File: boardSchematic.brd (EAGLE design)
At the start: 100 x 80 mm, 63 parts, among them IC2 TP4056, Q1 BC817-40SMD, Q2 BC817-40SMD, Q3 BC817-40SMD

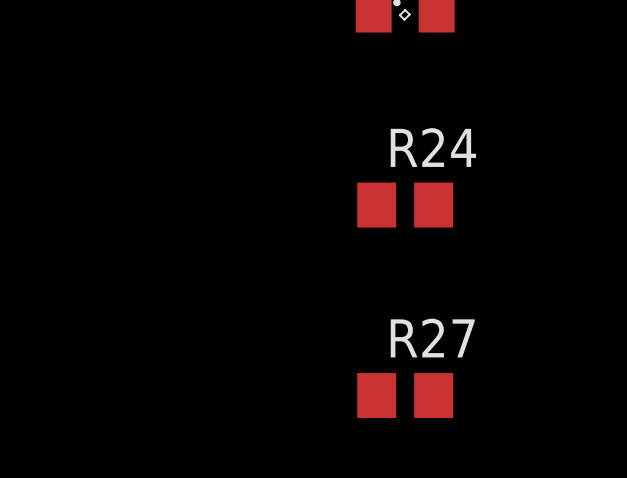
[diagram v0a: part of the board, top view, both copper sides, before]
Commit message: Added on/off switch
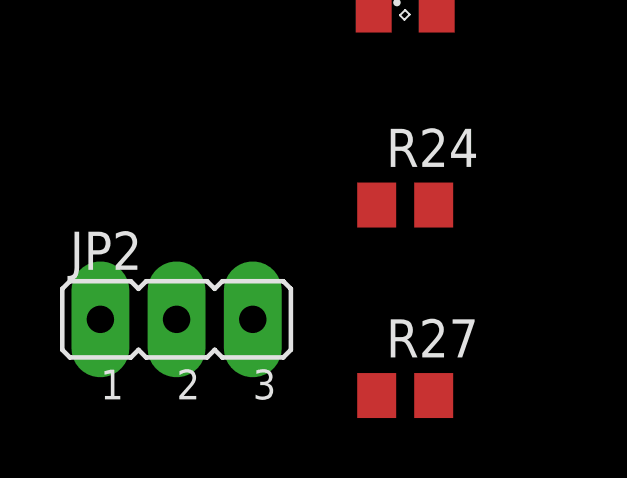
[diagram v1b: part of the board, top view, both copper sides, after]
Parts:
- added JP2: (no value), jumper:JP2
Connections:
- new net N$28: JP2.2, PAD1.1
- net VCC: now also JP2.1; no longer PAD1.1
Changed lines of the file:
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@@
 <element name="R24" library="rcl" package="R0805" value="103" x="-193.04" y="-275.59"/>
 <element name="R27" library="rcl" package="R0805" value="103" x="-193.04" y="-281.94"/>
+<element name="JP2" library="jumper" package="JP2" value="" x="-200.66" y="-279.4"/>
 </elements>
 <signals>
@@
 </signal>
 <signal name="VCC">
-<contactref element="PAD1" pad="1"/>
 <contactref element="U1" pad="3"/>
 <contactref element="C1" pad="1"/>
@@
 <contactref element="R17" pad="1"/>
 <contactref element="SG1" pad="+"/>
+<contactref element="JP2" pad="1"/>
+<wire x1="-168.91" y1="-214.63" x2="-203.2" y2="-279.4" width="0" layer="19" extent="1-1"/>
 <wire x1="-179.222" y1="-179.07" x2="-168.91" y2="-214.63" width="0" layer="19" extent="1-1"/>
 <wire x1="-179.222" y1="-173.99" x2="-179.222" y2="-179.07" width="0" layer="19" extent="1-1"/>
@@
 <wire x1="-25.08" y1="34.29" x2="-48.05" y2="-6.985" width="0" layer="19" extent="1-1"/>
 <wire x1="-14.1986" y1="32.4612" x2="-25.08" y2="34.29" width="0" layer="19" extent="1-1"/>
-<wire x1="-40.64" y1="44.45" x2="-25.08" y2="34.29" width="0" layer="19" extent="1-1"/>
 </signal>
 <signal name="+5V">
@@
 <wire x1="-186.055" y1="-235.0262" x2="-194.09" y2="-269.24" width="0" layer="19" extent="1-1"/>
 </signal>
+<signal name="N$28">
+<contactref element="JP2" pad="2"/>
+<contactref element="PAD1" pad="1"/>
+<wire x1="-40.64" y1="44.45" x2="-200.66" y2="-279.4" width="0" layer="19" extent="1-1"/>
+</signal>
 </signals>

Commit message: First guess of routing
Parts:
- removed LED1: RD, led:SML0805
- removed LED2, LED4: GR, led:SML0805
- removed R10, R9: 103, rcl:R0805
- removed R19, R20, R21, R23: 102, rcl:R0805
- moved JP2 443.0 mm to (68.6, 72.4)
- moved R24 366.0 mm to (25.6, 17.9)
- moved R27 363.6 mm to (30.6, 4.81), turned to 180 degrees
- moved Q3 361.4 mm to (19.3, 69.2)
- moved R26 356.1 mm to (35.6, 10.2)
- moved Q1 355.5 mm to (89.6, 40.0)
- moved R18 350.7 mm to (95.6, 40.6)
- moved C7 350.6 mm to (41.9, 11.4)
- moved R17 344.3 mm to (94.9, 36.2)
- moved C6 342.9 mm to (41.9, 7.62)
- moved LED8 340.5 mm to (12.2, 2.43)
- moved SG1 339.3 mm to (9.43, 71.6)
- moved U$2 332.8 mm to (34.9, 18.1)
- moved LED7 331.4 mm to (91.5, 53.1), turned to 270 degrees
- moved Q4 329.7 mm to (41.6, 1.54)
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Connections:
- removed net N$1: Q2.B, R21.2
- removed net N$10: IC2.6, LED2.C
- removed net N$2: LED1.A, R9.1
- removed net N$21: Q3.B, R23.2
- removed net N$26: LED4.A, R20.1
- removed net N$29: MEGA328.2, R20.2
- removed net N$4: Q1.B, R19.2
- removed net N$6: LED2.A, R10.1
- removed net N$8: IC2.7, LED1.C
- net BZR: now also Q3.B; no longer R23.1
- net GND: no longer LED4.C
- net GR: now also Q2.B; no longer R21.1
- net N$14: no longer R10.2, R9.2
- net RD: now also Q1.B; no longer R19.1
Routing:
- net N$1: track 0.00 -> 136.0 mm
- net N$2: track 0.00 -> 96.0 mm
- net N$4: track 0.00 -> 84.0 mm
- net +3V3: track 0.00 -> 16.4 mm
- net GND: track 0.00 -> 13.2 mm

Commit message: Test 2
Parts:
- moved C4 23.4 mm to (72.5, 75.4), turned to 90 degrees
- moved R2 16.0 mm to (83.0, 71.9)
- moved PAD2 13.6 mm to (77.4, 76.9)
- moved JP2 12.7 mm to (78.8, 64.7)
- moved USB1 12.2 mm to (92.0, 73.5)
- moved PAD1 11.5 mm to (75.9, 70.2)
- moved C5 10.9 mm to (63.8, 63.7), turned to 180 degrees
- moved IC2 9.68 mm to (68.6, 68.0)
- moved R8 6.13 mm to (63.1, 69.6), turned to 270 degrees
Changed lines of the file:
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@@
 <element name="MEGA328" library="avr-4" package="TQFP32-08" value="MEGA48/88/168-AU" x="30.02" y="46.96"/>
 <element name="JP1" library="avr-4" package="AVR-ISP-10" value="AVR-ISP-10" x="51.53" y="46.66"/>
-<element name="PAD1" library="wirepad" package="SMD2,54-5,08" value="3.7V batt" x="80.28" y="59.61" rot="R90"/>
-<element name="PAD2" library="wirepad" package="SMD2,54-5,08" value="" x="80.28" y="63.69" rot="R270"/>
+<element name="PAD1" library="wirepad" package="SMD2,54-5,08" value="3.7V batt" x="75.8858" y="70.2272" rot="R90"/>
+<element name="PAD2" library="wirepad" package="SMD2,54-5,08" value="" x="77.359" y="76.9234" rot="R270"/>
 <element name="R1" library="rcl" package="R0805" value="103" x="75.5" y="28.56"/>
 <element name="R13" library="rcl" package="R1206" value="0" x="57.61" y="20.16"/>
@@
 </element>
 <element name="USB-TTL1" library="dp_devices" package="M1X6_MALE_RIGHT_ANGLED_SMD" value="CON_HEADER_1X06-SMD-RIGHT-ANGLED" x="89.04" y="1.73" rot="R180"/>
-<element name="IC2" library="TP4056" package="SOP-8" value="TP4056" x="69.85" y="58.42"/>
-<element name="USB1" library="dp_devices" package="CONN_USB_MINI-B" value="CON-USB-F-MINI-B" x="79.74" y="73.58" rot="R90"/>
-<element name="R2" library="rcl" package="R1210W" value="0.4R" x="67.31" y="68.58"/>
-<element name="R8" library="rcl" package="R0805" value="122" x="63.5" y="63.5"/>
-<element name="C4" library="rcl" package="C1210" value="10uF" x="73.66" y="52.07"/>
-<element name="C5" library="rcl" package="C1210" value="10uF" x="67.31" y="53.34"/>
+<element name="IC2" library="TP4056" package="SOP-8" value="TP4056" x="68.6308" y="68.0212"/>
+<element name="USB1" library="dp_devices" package="CONN_USB_MINI-B" value="CON-USB-F-MINI-B" x="91.9574" y="73.453" rot="R90"/>
+<element name="R2" library="rcl" package="R1210W" value="0.4R" x="82.9818" y="71.882"/>
+<element name="R8" library="rcl" package="R0805" value="122" x="63.119" y="69.6214" rot="R270"/>
+<element name="C4" library="rcl" package="C1210" value="10uF" x="72.517" y="75.438" rot="R90"/>
+<element name="C5" library="rcl" package="C1210" value="10uF" x="63.8302" y="63.6778" rot="R180"/>
 <element name="RF" library="pinhead" package="2X04" value="" x="31.53" y="34.42"/>
 <element name="R11" library="rcl" package="R0805" value="103" x="22.91" y="28.34"/>
@@
 <element name="R24" library="rcl" package="R0805" value="103" x="25.59" y="17.89"/>
 <element name="R27" library="rcl" package="R0805" value="103" x="30.59" y="4.81" rot="R180"/>
-<element name="JP2" library="jumper" package="JP2" value="" x="68.58" y="72.39"/>
+<element name="JP2" library="jumper" package="JP2" value="" x="78.7654" y="64.7446"/>
 </elements>
 <signals>
@@
 <wire x1="25.7274" y1="46.56" x2="28.8528" y2="46.56" width="0.4064" layer="1"/>
 <wire x1="28.8528" y1="46.56" x2="29.6528" y2="47.36" width="0.4064" layer="1"/>
-<wire x1="80.28" y1="63.69" x2="76.64" y2="75.18" width="0" layer="19" extent="1-1"/>
-<wire x1="75.06" y1="52.07" x2="80.28" y2="63.69" width="0" layer="19" extent="1-1"/>
-<wire x1="68.71" y1="53.34" x2="75.06" y2="52.07" width="0" layer="19" extent="1-1"/>
-<wire x1="67.1" y1="57.785" x2="68.71" y2="53.34" width="0" layer="19" extent="1-1"/>
-<wire x1="67.1" y1="60.325" x2="67.1" y2="57.785" width="0" layer="19" extent="1-1"/>
-<wire x1="62.55" y1="63.5" x2="67.1" y2="60.325" width="0" layer="19" extent="1-1"/>
-<wire x1="56.61" y1="47.93" x2="68.71" y2="53.34" width="0" layer="19" extent="1-1"/>
+<wire x1="77.359" y1="76.9234" x2="88.8574" y2="75.053" width="0" layer="19" extent="1-1"/>
+<wire x1="72.517" y1="76.838" x2="77.359" y2="76.9234" width="0" layer="19" extent="1-1"/>
+<wire x1="62.4302" y1="63.6778" x2="72.517" y2="76.838" width="0" layer="19" extent="1-1"/>
+<wire x1="65.8808" y1="67.3862" x2="62.4302" y2="63.6778" width="0" layer="19" extent="1-1"/>
+<wire x1="65.8808" y1="69.9262" x2="65.8808" y2="67.3862" width="0" layer="19" extent="1-1"/>
+<wire x1="63.119" y1="70.5714" x2="65.8808" y2="69.9262" width="0" layer="19" extent="1-1"/>
+<wire x1="56.61" y1="47.93" x2="62.4302" y2="63.6778" width="0" layer="19" extent="1-1"/>
 <wire x1="54.07" y1="47.93" x2="56.61" y2="47.93" width="0" layer="19" extent="1-1"/>
 <wire x1="51.53" y1="47.93" x2="54.07" y2="47.93" width="0" layer="19" extent="1-1"/>
@@
 <wire x1="27.72" y1="33.15" x2="28.8528" y2="46.56" width="0" layer="19" extent="1-1"/>
 <wire x1="16.19" y1="36.35" x2="27.72" y2="33.15" width="0" layer="19" extent="1-1"/>
-<wire x1="83.71" y1="38.91" x2="75.06" y2="52.07" width="0" layer="19" extent="1-1"/>
+<wire x1="83.71" y1="38.91" x2="72.517" y2="76.838" width="0" layer="19" extent="1-1"/>
 <wire x1="90.54" y1="38.89" x2="83.71" y2="38.91" width="0" layer="19" extent="1-1"/>
 <wire x1="72.71" y1="34.75" x2="83.71" y2="38.91" width="0" layer="19" extent="1-1"/>
@@
 <contactref element="SG1" pad="+"/>
 <contactref element="JP2" pad="1"/>
-<wire x1="72.6" y1="56.515" x2="66.04" y2="72.39" width="0" layer="19" extent="1-1"/>
-<wire x1="72.26" y1="52.07" x2="72.6" y2="56.515" width="0" layer="19" extent="1-1"/>
-<wire x1="64.1914" y1="30.3812" x2="72.26" y2="52.07" width="0" layer="19" extent="1-1"/>
+<wire x1="71.3808" y1="66.1162" x2="76.2254" y2="64.7446" width="0" layer="19" extent="1-1"/>
+<wire x1="72.517" y1="74.038" x2="71.3808" y2="66.1162" width="0" layer="19" extent="1-1"/>
+<wire x1="64.1914" y1="30.3812" x2="72.517" y2="74.038" width="0" layer="19" extent="1-1"/>
 <wire x1="64.47" y1="25.24" x2="64.1914" y2="30.3812" width="0" layer="19" extent="1-1"/>
-<wire x1="94.168" y1="40.58" x2="72.26" y2="52.07" width="0" layer="19" extent="1-1"/>
+<wire x1="94.168" y1="40.58" x2="72.517" y2="74.038" width="0" layer="19" extent="1-1"/>
 <wire x1="93.438" y1="36.2" x2="94.168" y2="40.58" width="0" layer="19" extent="1-1"/>
-<wire x1="13.24" y1="71.62" x2="66.04" y2="72.39" width="0" layer="19" extent="1-1"/>
+<wire x1="13.24" y1="71.62" x2="76.2254" y2="64.7446" width="0" layer="19" extent="1-1"/>
 <wire x1="4.658" y1="38.2" x2="13.24" y2="71.62" width="0" layer="19" extent="1-1"/>
 <wire x1="9.548" y1="35.66" x2="4.658" y2="38.2" width="0" layer="19" extent="1-1"/>
@@
 <contactref element="R2" pad="2"/>
 <contactref element="USB1" pad="VUSB"/>
-<wire x1="68.809" y1="68.58" x2="76.64" y2="71.98" width="0" layer="19" extent="1-1"/>
+<wire x1="84.4808" y1="71.882" x2="88.8574" y2="71.853" width="0" layer="19" extent="1-1"/>
 </signal>
 <signal name="N$14">
@@
 <contactref element="IC2" pad="4"/>
 <contactref element="C5" pad="1"/>
-<wire x1="72.6" y1="60.325" x2="65.811" y2="68.58" width="0" layer="19" extent="1-1"/>
-<wire x1="67.1" y1="56.515" x2="72.6" y2="60.325" width="0" layer="19" extent="1-1"/>
-<wire x1="65.91" y1="53.34" x2="67.1" y2="56.515" width="0" layer="19" extent="1-1"/>
+<wire x1="71.3808" y1="69.9262" x2="81.4828" y2="71.882" width="0" layer="19" extent="1-1"/>
+<wire x1="65.8808" y1="66.1162" x2="71.3808" y2="69.9262" width="0" layer="19" extent="1-1"/>
+<wire x1="65.2302" y1="63.6778" x2="65.8808" y2="66.1162" width="0" layer="19" extent="1-1"/>
 </signal>
 <signal name="N$11">
 <contactref element="IC2" pad="2"/>
 <contactref element="R8" pad="2"/>
-<wire x1="67.1" y1="59.055" x2="64.45" y2="63.5" width="0" layer="19" extent="1-1"/>
+<wire x1="65.8808" y1="68.6562" x2="63.119" y2="68.6714" width="0" layer="19" extent="1-1"/>
 </signal>
 <signal name="SCK">
@@
 <contactref element="JP2" pad="2"/>
 <contactref element="PAD1" pad="1"/>
-<wire x1="80.28" y1="59.61" x2="68.58" y2="72.39" width="0" layer="19" extent="1-1"/>
+<wire x1="75.8858" y1="70.2272" x2="78.7654" y2="64.7446" width="0" layer="19" extent="1-1"/>
 </signal>
 <signal name="RD">

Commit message: Test3
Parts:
- moved R3 26.9 mm to (48.7, 24.7)
- moved C1 21.5 mm to (53.7, 7.26)
- moved C3 20.9 mm to (57.6, 10.5)
- moved R5 19.9 mm to (67.1, 17.8)
- moved R4 19.5 mm to (75.8, 11.0)
- moved R1 18.1 mm to (68.3, 12.0)
- moved R6 17.9 mm to (82.8, 11.9)
- moved R22 15.4 mm to (71.1, 5.07)
- moved C2 14.8 mm to (50.6, 13.5)
- moved R13 14.7 mm to (63.5, 6.70)
- moved U1 14.0 mm to (56.6, 20.5)
- moved R7 9.59 mm to (59.4, 36.1)
